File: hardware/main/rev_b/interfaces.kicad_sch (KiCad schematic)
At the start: 12 parts, among them U50 TCAN3413DR, U51 MCP2518FD-H/QBB, Y50 40MHz ABM8G

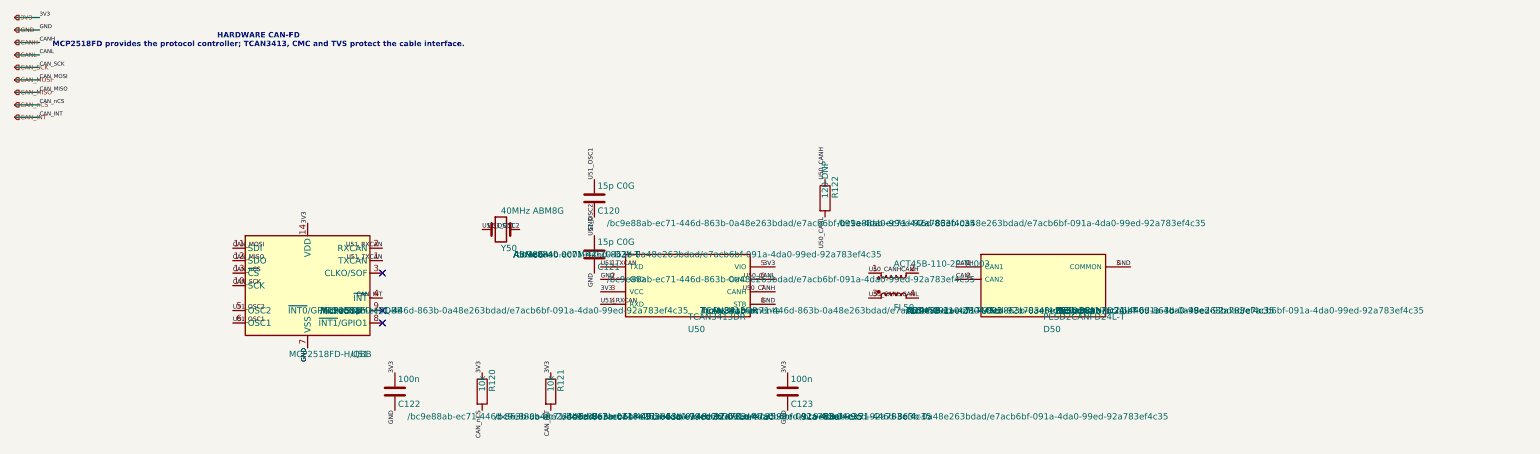
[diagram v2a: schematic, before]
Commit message: build: route and validate rev-b boards
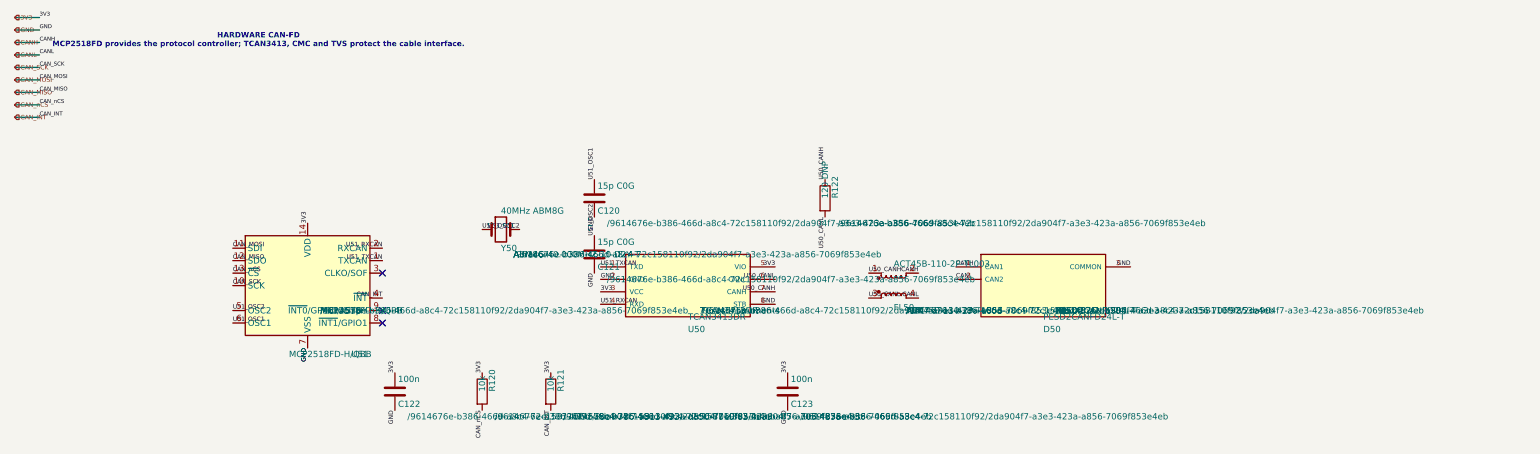
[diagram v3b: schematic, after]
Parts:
- C120, C121, C122, C123, D50, FL50, R120, R121, R122, U50, U51, Y50: hierarchy_path /bc9e88ab-ec71-446d-863b-0a48e263bdad/e7acb6bf-091a-4da0-99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 -> /9614676e-b386-466d-a8c4-72c158110f92/2da904f7-a3e3-423a-a8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
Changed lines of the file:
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@@
 			)
 		)
-		(property "hierarchy_path" "/bc9e88ab-ec71-446d-863b-0a48e263bdad/e7acb6bf-091a-4da0-99ed-92a783ef4c35"
+		(property "hierarchy_path" "/9614676e-b386-466d-a8c4-72c158110f92/2da904f7-a3e3-423a-a856-7069f853e4eb"
 			(at 82.55 80.0099 0)
 			(effects
@@
 		(instances
 			(project "main_rev_b"
-				(path "/bc9e88ab-ec71-446d-863b-0a48e263bdad/e7acb6bf-091a-4da0-99ed-92a783ef4c35"
+				(path "/9614676e-b386-466d-a8c4-72c158110f92/2da904f7-a3e3-423a-a856-7069f853e4eb"
 					(reference "U51")
 					(unit 1)
@@
 			)
 		)
-		(property "hierarchy_path" "/bc9e88ab-ec71-446d-863b-0a48e263bdad/e7acb6bf-091a-4da0-99ed-92a783ef4c35"
+		(property "hierarchy_path" "/9614676e-b386-466d-a8c4-72c158110f92/2da904f7-a3e3-423a-a856-7069f853e4eb"
 			(at 121.92 68.5799 0)
 			(effects
@@
 		(instances
 			(project "main_rev_b"
-				(path "/bc9e88ab-ec71-446d-863b-0a48e263bdad/e7acb6bf-091a-4da0-99ed-92a783ef4c35"
+				(path "/9614676e-b386-466d-a8c4-72c158110f92/2da904f7-a3e3-423a-a856-7069f853e4eb"
 					(reference "Y50")
 					(unit 1)
@@
 			)
 		)
-		(property "hierarchy_path" "/bc9e88ab-ec71-446d-863b-0a48e263bdad/e7acb6bf-091a-4da0-99ed-92a783ef4c35"
+		(property "hierarchy_path" "/9614676e-b386-466d-a8c4-72c158110f92/2da904f7-a3e3-423a-a856-7069f853e4eb"
 			(at 140.97 62.2299 0)
 			(effects
@@
 		(instances
 			(project "main_rev_b"
-				(path "/bc9e88ab-ec71-446d-863b-0a48e263bdad/e7acb6bf-091a-4da0-99ed-92a783ef4c35"
+				(path "/9614676e-b386-466d-a8c4-72c158110f92/2da904f7-a3e3-423a-a856-7069f853e4eb"
 					(reference "C120")
 					(unit 1)
@@
 			)
 		)
-		(property "hierarchy_path" "/bc9e88ab-ec71-446d-863b-0a48e263bdad/e7acb6bf-091a-4da0-99ed-92a783ef4c35"
+		(property "hierarchy_path" "/9614676e-b386-466d-a8c4-72c158110f92/2da904f7-a3e3-423a-a856-7069f853e4eb"
 			(at 140.97 73.6599 0)
 			(effects
@@
 		(instances
 			(project "main_rev_b"
-				(path "/bc9e88ab-ec71-446d-863b-0a48e263bdad/e7acb6bf-091a-4da0-99ed-92a783ef4c35"
+				(path "/9614676e-b386-466d-a8c4-72c158110f92/2da904f7-a3e3-423a-a856-7069f853e4eb"
 					(reference "C121")
 					(unit 1)
@@
 			)
 		)
-		(property "hierarchy_path" "/bc9e88ab-ec71-446d-863b-0a48e263bdad/e7acb6bf-091a-4da0-99ed-92a783ef4c35"
+		(property "hierarchy_path" "/9614676e-b386-466d-a8c4-72c158110f92/2da904f7-a3e3-423a-a856-7069f853e4eb"
 			(at 100.33 101.5999 0)
 			(effects
@@
 		(instances
 			(project "main_rev_b"
-				(path "/bc9e88ab-ec71-446d-863b-0a48e263bdad/e7acb6bf-091a-4da0-99ed-92a783ef4c35"
+				(path "/9614676e-b386-466d-a8c4-72c158110f92/2da904f7-a3e3-423a-a856-7069f853e4eb"
 					(reference "C122")
 					(unit 1)
@@
 			)
 		)
-		(property "hierarchy_path" "/bc9e88ab-ec71-446d-863b-0a48e263bdad/e7acb6bf-091a-4da0-99ed-92a783ef4c35"
+		(property "hierarchy_path" "/9614676e-b386-466d-a8c4-72c158110f92/2da904f7-a3e3-423a-a856-7069f853e4eb"
 			(at 118.11 101.5999 0)
 			(effects
@@
 		(instances
 			(project "main_rev_b"
-				(path "/bc9e88ab-ec71-446d-863b-0a48e263bdad/e7acb6bf-091a-4da0-99ed-92a783ef4c35"
+				(path "/9614676e-b386-466d-a8c4-72c158110f92/2da904f7-a3e3-423a-a856-7069f853e4eb"
 					(reference "R120")
 					(unit 1)
@@
 			)
 		)
-		(property "hierarchy_path" "/bc9e88ab-ec71-446d-863b-0a48e263bdad/e7acb6bf-091a-4da0-99ed-92a783ef4c35"
+		(property "hierarchy_path" "/9614676e-b386-466d-a8c4-72c158110f92/2da904f7-a3e3-423a-a856-7069f853e4eb"
 			(at 132.08 101.5999 0)
 			(effects
@@
 		(instances
 			(project "main_rev_b"
-				(path "/bc9e88ab-ec71-446d-863b-0a48e263bdad/e7acb6bf-091a-4da0-99ed-92a783ef4c35"
+				(path "/9614676e-b386-466d-a8c4-72c158110f92/2da904f7-a3e3-423a-a856-7069f853e4eb"
 					(reference "R121")
 					(unit 1)
@@
 			)
 		)
-		(property "hierarchy_path" "/bc9e88ab-ec71-446d-863b-0a48e263bdad/e7acb6bf-091a-4da0-99ed-92a783ef4c35"
+		(property "hierarchy_path" "/9614676e-b386-466d-a8c4-72c158110f92/2da904f7-a3e3-423a-a856-7069f853e4eb"
 			(at 160.02 80.0099 0)
 			(effects
@@
 		(instances
 			(project "main_rev_b"
-				(path "/bc9e88ab-ec71-446d-863b-0a48e263bdad/e7acb6bf-091a-4da0-99ed-92a783ef4c35"
+				(path "/9614676e-b386-466d-a8c4-72c158110f92/2da904f7-a3e3-423a-a856-7069f853e4eb"
 					(reference "U50")
 					(unit 1)
@@
 			)
 		)
-		(property "hierarchy_path" "/bc9e88ab-ec71-446d-863b-0a48e263bdad/e7acb6bf-091a-4da0-99ed-92a783ef4c35"
+		(property "hierarchy_path" "/9614676e-b386-466d-a8c4-72c158110f92/2da904f7-a3e3-423a-a856-7069f853e4eb"
 			(at 180.34 101.5999 0)
 			(effects
@@
 		(instances
 			(project "main_rev_b"
-				(path "/bc9e88ab-ec71-446d-863b-0a48e263bdad/e7acb6bf-091a-4da0-99ed-92a783ef4c35"
+				(path "/9614676e-b386-466d-a8c4-72c158110f92/2da904f7-a3e3-423a-a856-7069f853e4eb"
 					(reference "C123")
 					(unit 1)
@@
 			)
 		)
-		(property "hierarchy_path" "/bc9e88ab-ec71-446d-863b-0a48e263bdad/e7acb6bf-091a-4da0-99ed-92a783ef4c35"
+		(property "hierarchy_path" "/9614676e-b386-466d-a8c4-72c158110f92/2da904f7-a3e3-423a-a856-7069f853e4eb"
 			(at 201.93 80.0099 0)
 			(effects
@@
 		(instances
 			(project "main_rev_b"
-				(path "/bc9e88ab-ec71-446d-863b-0a48e263bdad/e7acb6bf-091a-4da0-99ed-92a783ef4c35"
+				(path "/9614676e-b386-466d-a8c4-72c158110f92/2da904f7-a3e3-423a-a856-7069f853e4eb"
 					(reference "FL50")
 					(unit 1)
@@
 			)
 		)
-		(property "hierarchy_path" "/bc9e88ab-ec71-446d-863b-0a48e263bdad/e7acb6bf-091a-4da0-99ed-92a783ef4c35"
+		(property "hierarchy_path" "/9614676e-b386-466d-a8c4-72c158110f92/2da904f7-a3e3-423a-a856-7069f853e4eb"
 			(at 187.96 62.2299 0)
 			(effects
@@
 		(instances
 			(project "main_rev_b"
-				(path "/bc9e88ab-ec71-446d-863b-0a48e263bdad/e7acb6bf-091a-4da0-99ed-92a783ef4c35"
+				(path "/9614676e-b386-466d-a8c4-72c158110f92/2da904f7-a3e3-423a-a856-7069f853e4eb"
 					(reference "R122")
 					(unit 1)
@@
 			)
 		)
-		(property "hierarchy_path" "/bc9e88ab-ec71-446d-863b-0a48e263bdad/e7acb6bf-091a-4da0-99ed-92a783ef4c35"
+		(property "hierarchy_path" "/9614676e-b386-466d-a8c4-72c158110f92/2da904f7-a3e3-423a-a856-7069f853e4eb"
 			(at 232.41 80.0099 0)
 			(effects
@@
 		(instances
 			(project "main_rev_b"
-				(path "/bc9e88ab-ec71-446d-863b-0a48e263bdad/e7acb6bf-091a-4da0-99ed-92a783ef4c35"
+				(path "/9614676e-b386-466d-a8c4-72c158110f92/2da904f7-a3e3-423a-a856-7069f853e4eb"
 					(reference "D50")
 					(unit 1)
